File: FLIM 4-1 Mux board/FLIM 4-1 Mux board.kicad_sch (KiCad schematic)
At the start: 76 parts, among them J1 Conn_01x14_Pin, J10 Conn_01x03_Socket, J11 Conn_01x03_Socket, J12 Conn_01x03_Socket, J13 Conn_01x03_Socket, J14 Conn_01x03_Pin, J15 Conn_01x03_Pin, J16 Conn_01x03_Pin, J17 Conn_01x03_Pin, J2 Conn_01x14_Pin, J3 Conn_01x05_Pin, J4 Conn_Coaxial, J5 Conn_Coaxial, J6 Conn_Coaxial, J7 Conn_Coaxial, J8 Conn_Coaxial, J9 Barrel_Jack, SW1 SW_Push_LED, SW2 SW_Push_LED, SW3 SW_Push_LED, SW4 SW_Push_LED, U1 SPDT RF switch, U2 CD74HCT175M96, U3 ADM7150ARDZ-5.0, U4 Itsy_Bitsy_32u4, U5 SPDT RF switch, U6 SPDT RF switch

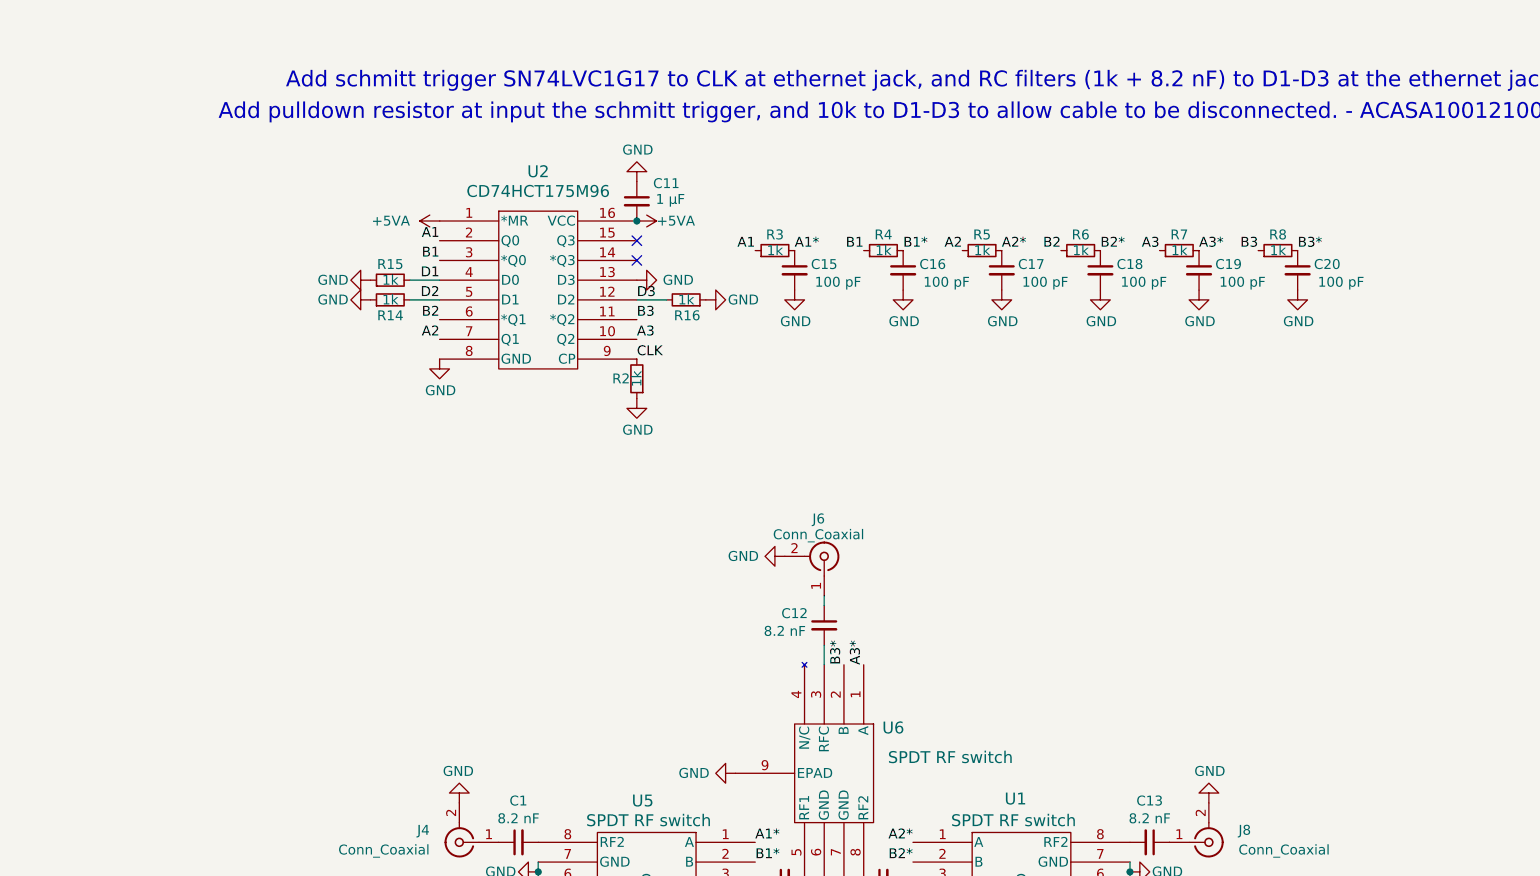
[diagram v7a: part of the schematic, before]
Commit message: Switch to scmitt triggered flip flops
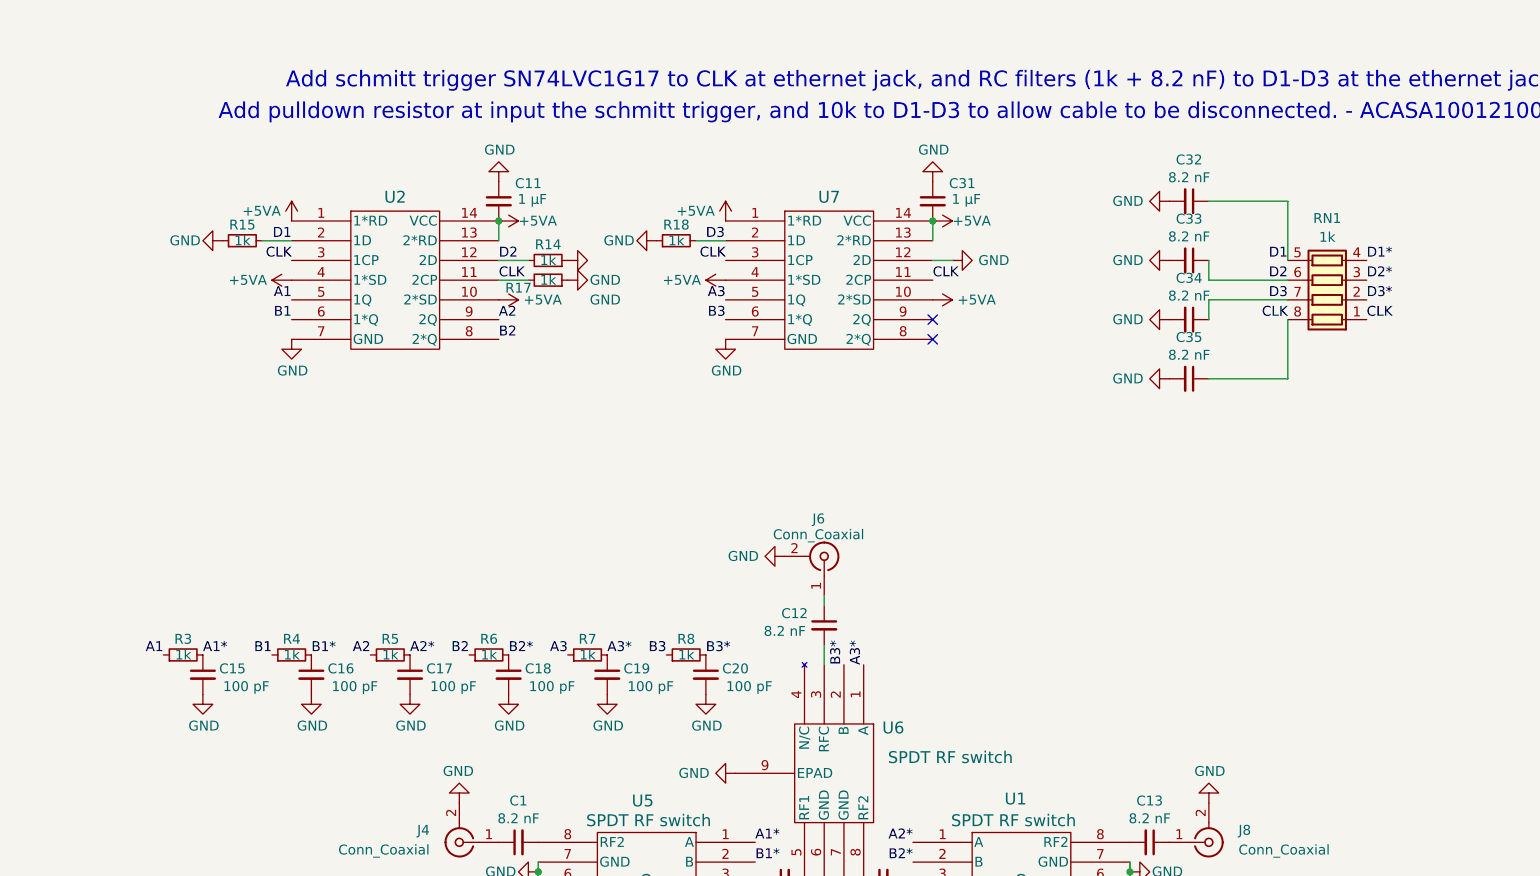
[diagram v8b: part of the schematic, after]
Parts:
- removed R16, R2: 1k, Resistor_SMD:R_0603_1608Metric, symbol Device:R_Small
- removed U2: CD74HCT175M96, Custom:74HCT175, symbol Custom:CD74HCT175M96
- added C31: 1 µF, Capacitor_SMD:C_0805_2012Metric, symbol Device:C_Small
- added C32, C33, C34, C35: 8.2 nF, Capacitor_SMD:C_0402_1005Metric, symbol Device:C_Small
- added R17, R18: 1k, Resistor_SMD:R_0603_1608Metric, symbol Device:R_Small
- added RN1: 1k, Resistor_SMD:R_Array_Convex_4x0603, symbol Device:R_Pack04
- added U2, U7: 74AHCT74D_118, Custom:74AHCT74D_118_NEX, symbol Custom:74AHCT74D_118
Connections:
- net +5VA: now also C31.2, U2.1 (1*RD), U2.10 (2*SD), U2.13 (2*RD), U2.14 (VCC), U2.4 (1*SD), U7.1 (1*RD), U7.10 (2*SD), U7.13 (2*RD), U7.14 (VCC), U7.4 (1*SD)
- net A1: now also U2.5 (1Q)
- net A2: now also U2.9 (2Q)
- net A3: now also U7.5 (1Q)
- net B1: now also U2.6 (1*Q)
- net B2: now also U2.8 (2*Q)
- net B3: now also U7.6 (1*Q)
- net CLK: now also C35.1, R17.2, RN1.1 (R1.1), RN1.8 (R1.2), U2.11 (2CP), U2.3 (1CP), U7.11 (2CP), U7.3 (1CP)
- net D1: now also C32.1, RN1.5 (R4.2), U2.2 (1D)
- net D2: now also C33.1, RN1.6 (R3.2), U2.12 (2D)
- net D3: now also C34.1, R18.2, RN1.7 (R2.2), U7.2 (1D)
- net GND: now also C31.1, C32.2, C33.2, C34.2, C35.2, R17.1, R18.1, U2.7 (GND), U7.12 (2D), U7.7 (GND)
- new net D1*: RN1.4 (R4.1)
- new net D2*: RN1.3 (R3.1)
- new net D3*: RN1.2 (R2.1)
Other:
- moved on the sheet: C11, C15, C16, C17, C18, C19, C20, R14, R15, R3, R4, R5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
